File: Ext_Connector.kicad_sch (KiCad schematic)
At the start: 0 parts

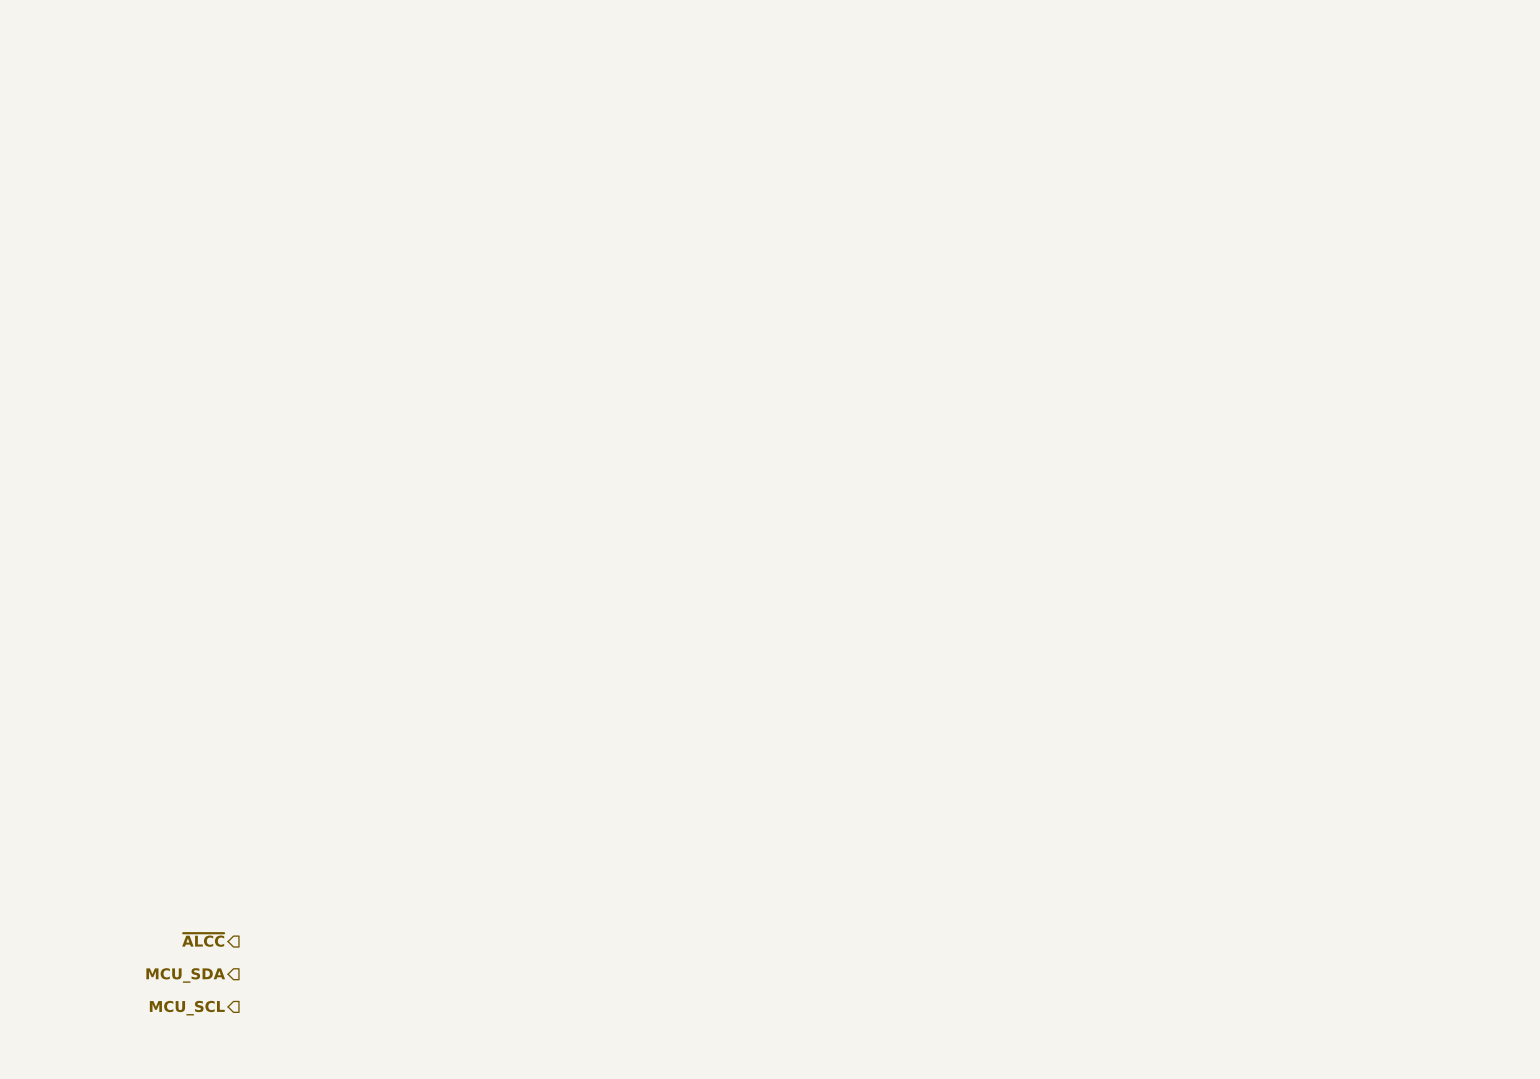
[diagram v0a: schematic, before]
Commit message: Assigned footprints
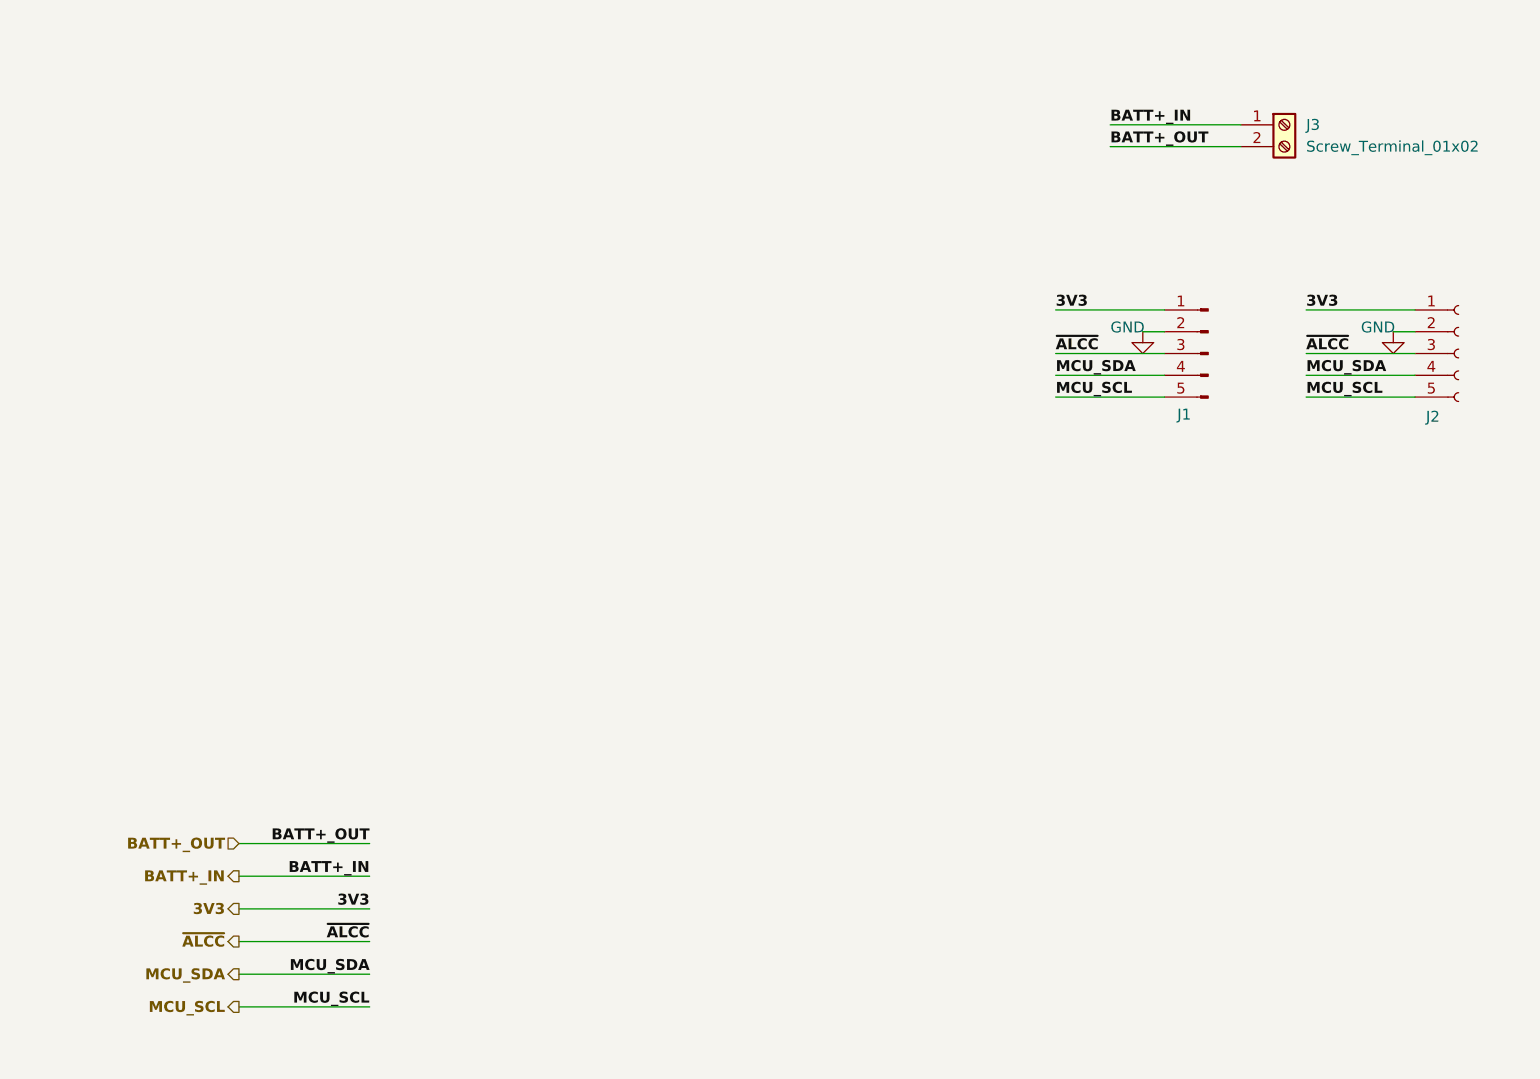
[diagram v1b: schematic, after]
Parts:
- added J1: Conn_01x05_Pin, PP_PoC:PinHeader_1x05_P2.54mm_Vertical, symbol PP_PoC:Conn_01x05_Pin
- added J2: Conn_01x05_Socket, PP_PoC:PinHeader_1x05_P2.54mm_Vertical, symbol PP_PoC:Conn_01x05_Socket
- added J3: Screw_Terminal_01x02, PP_PoC:2P_Screw_Terminal, symbol PP_PoC:Screw_Terminal_01x02
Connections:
- net MCU_SCL: now also J1.5 (Pin_5), J2.5 (Pin_5)
- net MCU_SDA: now also J1.4 (Pin_4), J2.4 (Pin_4)
- net ~{ALCC}: now also J1.3 (Pin_3), J2.3 (Pin_3)
- new net 3V3: J1.1 (Pin_1), J2.1 (Pin_1)
- new net BATT+_IN: J3.1 (Pin_1)
- new net BATT+_OUT: J3.2 (Pin_2)
- new net GND: J1.2 (Pin_2), J2.2 (Pin_2)

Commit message: Started routing
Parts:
- added JP1: Jumper_2_Open, PP_PoC:PinHeader_1x02_P2.54mm_Vertical, symbol PP_PoC:Jumper_2_Open
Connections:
- net MCU_SCL is gone; now on net GND: J1.5 (Pin_5), J2.5 (Pin_5)
- net BATT+_IN: now also JP1.2 (B)
- net GND: no longer J1.2 (Pin_2), J2.2 (Pin_2)
- net 3V3 renamed SCL
- net MCU_SDA renamed 3V3/5V
- net 3V3/5V: now also JP1.1 (A)
- new net SDA: J1.2 (Pin_2), J2.2 (Pin_2)
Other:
- moved on the sheet: J3
